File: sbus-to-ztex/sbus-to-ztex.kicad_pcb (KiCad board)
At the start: 4 copper layers, 99.7 x 83.8 mm, 37 parts, among them J1 Conn_01x06_Male, J2 47219-2001, J3 Conn_02x07_Odd_Even, J4 USB_B_Micro, J5 Conn_02x06_Odd_Even, U1 SN74CB3T16211DGGR, U2 SN74CB3T16211DGGR, U3 SN74CB3T16211DGGR, U4 SN74CB3T3125PW, U5 SN65220, U7 TPS2065

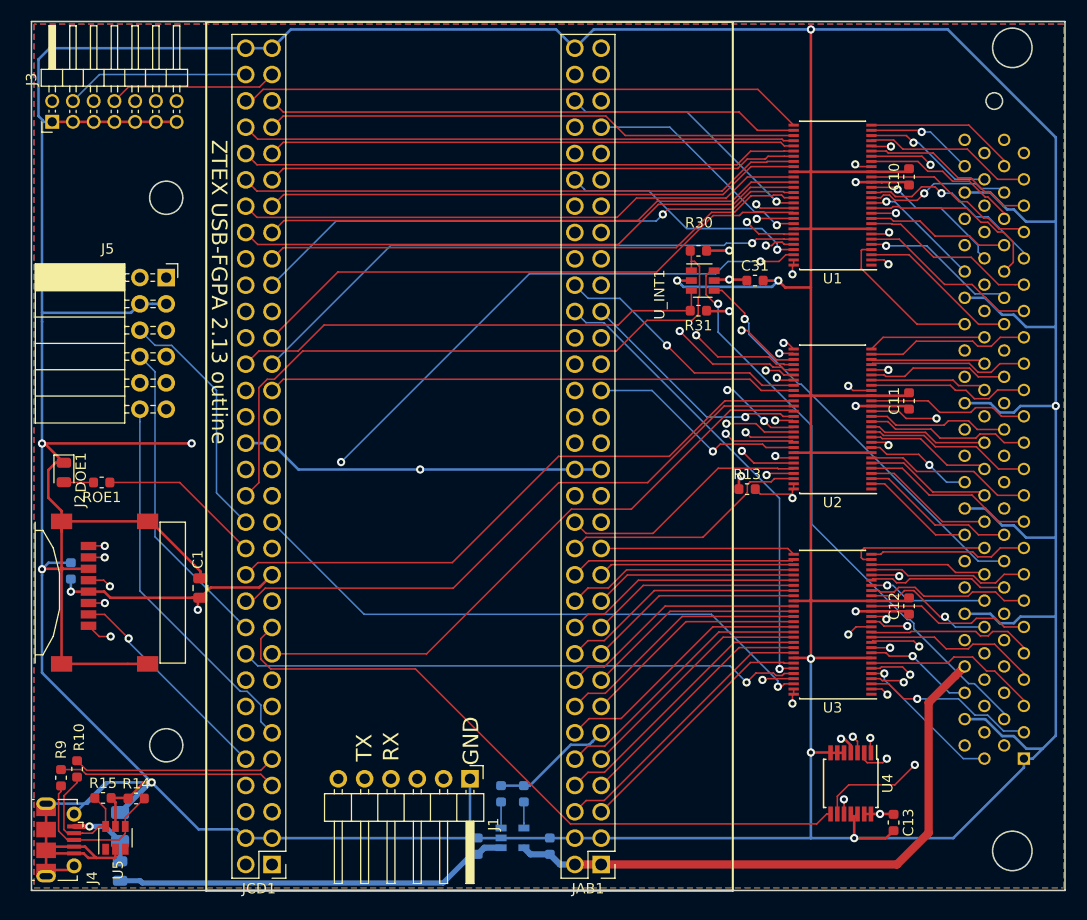
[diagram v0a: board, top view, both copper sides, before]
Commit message: fix footprints for SeeedStudio DRC results
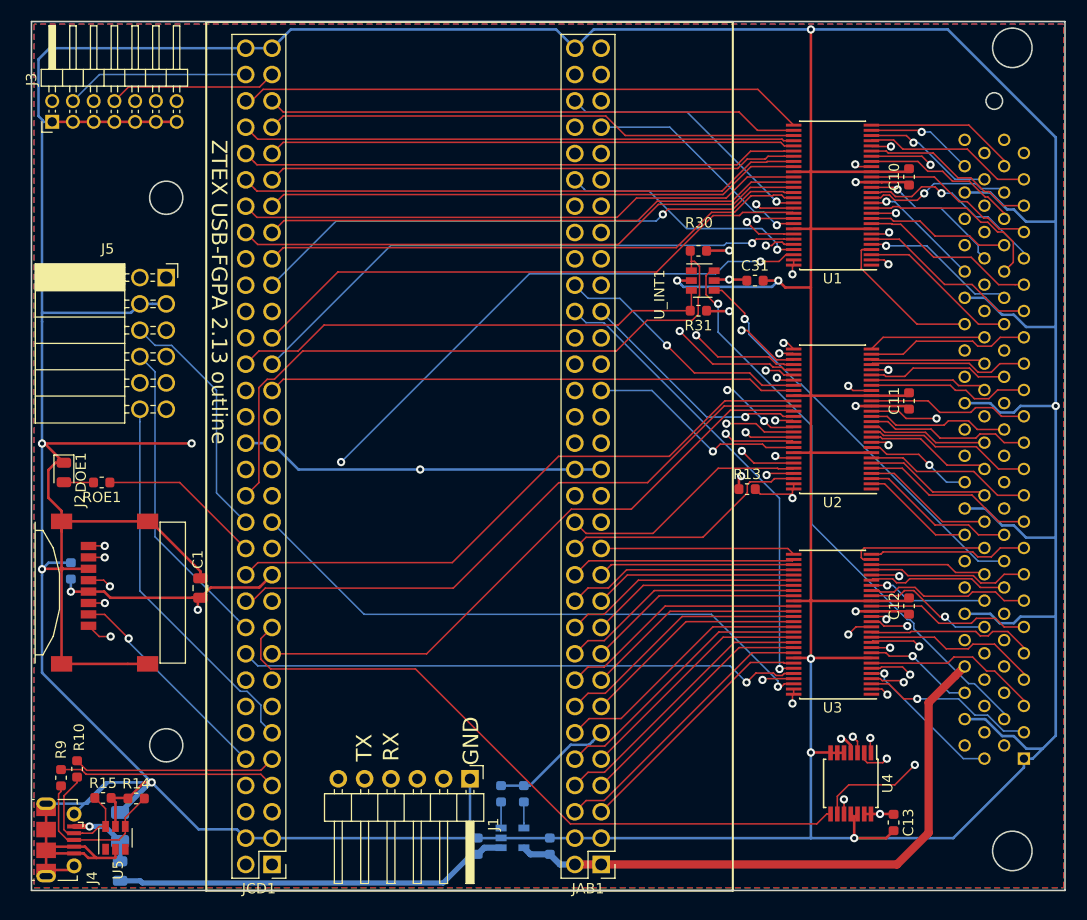
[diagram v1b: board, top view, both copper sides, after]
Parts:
- J3: footprint Connector_PinHeader_2.00mm:PinHeader_2x07_P2.00mm_Horizontal -> For_SeeedStudio:PinHeader_2x07_P2.00mm_Horizontal_For_SeeedStudio
- J5: footprint Connector_PinSocket_2.54mm:PinSocket_2x06_P2.54mm_Horizontal -> For_SeeedStudio:PinSocket_2x06_P2.54mm_Horizontal_For_SeeedStudio
- JAB1, JCD1: footprint Connector_PinHeader_2.54mm:PinHeader_2x32_P2.54mm_Vertical -> For_SeeedStudio:PinHeader_2x32_P2.54mm_Vertical_For_SeeedStudio
- U1, U2, U3: footprint Package_SO:TSSOP-56_6.1x14mm_P0.5mm -> For_SeeedStudio:TSSOP-56_6.1x14mm_P0.5mm_For_SeeedStudio

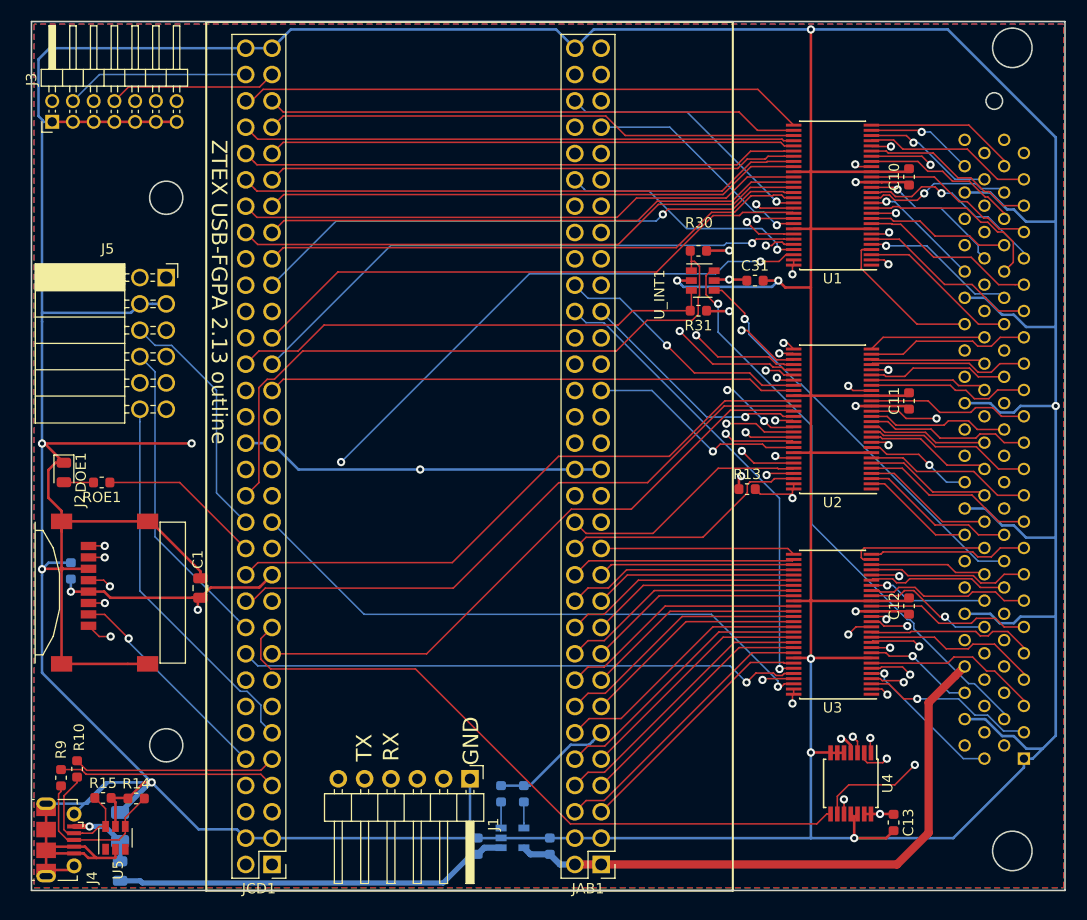
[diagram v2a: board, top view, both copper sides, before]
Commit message: update some MPN w/ SeeedStudio replacement
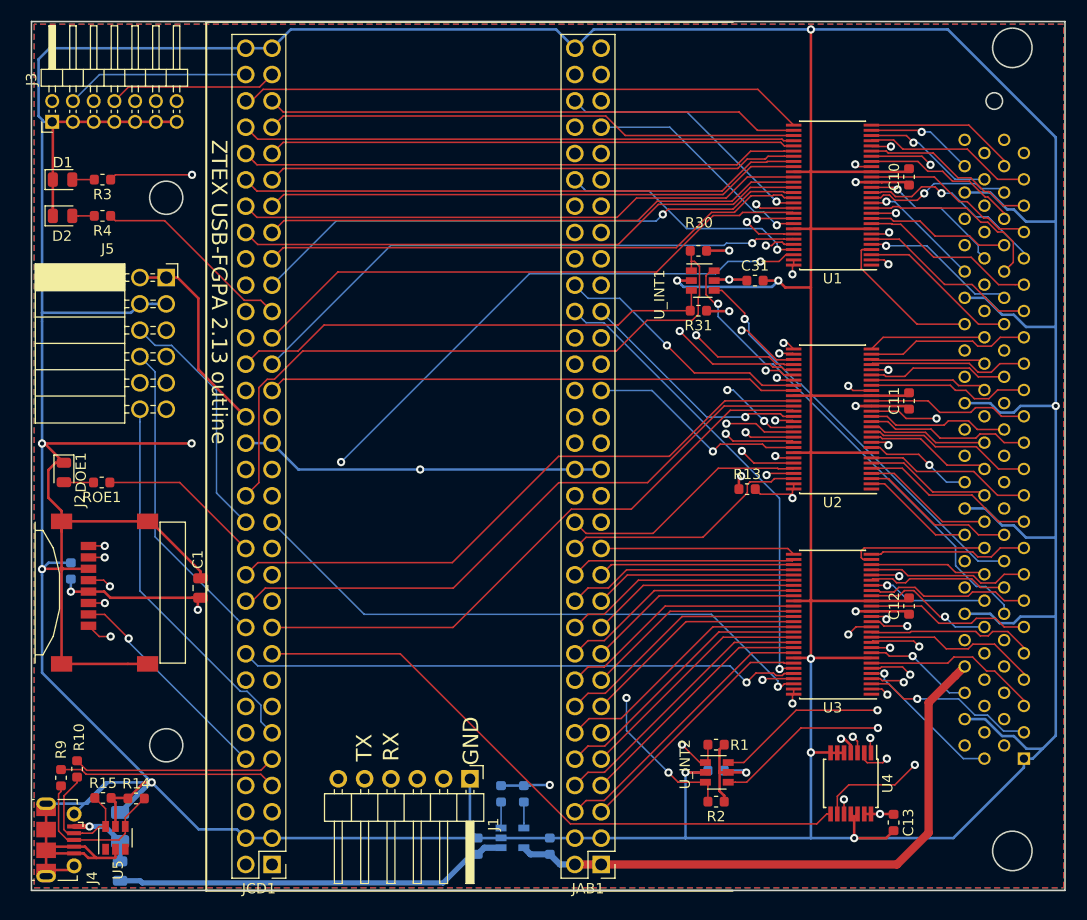
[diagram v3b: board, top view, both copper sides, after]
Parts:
- added C4: 100nF, Capacitor_SMD:C_0603_1608Metric, B.Cu at (163.0, 122.3)
- added D1: RED, LED_SMD:LED_0805_2012Metric, F.Cu at (100.0, 65.2)
- added D2: RED, LED_SMD:LED_0805_2012Metric, F.Cu at (100.0, 68.8)
- added R1: 10k, Resistor_SMD:R_0603_1608Metric, F.Cu at (163.0, 119.8)
- added R2: 10k, Resistor_SMD:R_0603_1608Metric, F.Cu at (163.0, 125.3)
- added R3: 549, Resistor_SMD:R_0603_1608Metric, F.Cu at (103.8, 65.2)
- added R4: 549, Resistor_SMD:R_0603_1608Metric, F.Cu at (103.8, 68.8)
- added U_INT2: 74LVC2G07, Package_TO_SOT_SMD:SOT-23-6, F.Cu at (163.1, 122.4)
- J1: footprint Connector_PinHeader_2.54mm:PinHeader_1x06_P2.54mm_Horizontal -> For_SeeedStudio:PinHeader_1x06_P2.54mm_Horizontal_For_SeeedStudio
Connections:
- JAB1 pad 11: +3V3 -> SBUS_3V3_INT[2]*
- JAB1 pad 49: +3V3 -> LED0
- JCD1 pad 17: SBUS_3V3_SIZ[0] -> SBUS_3V3_BG*
- JCD1 pad 19: SBUS_3V3_BG* -> SBUS_3V3_SIZ[0]
- JCD1 pad 23: +3V3 -> SBUS_3V3_INT[1]*
- JCD1 pad 30: SBUS_3V3_INT[1]* -> SBUS_3V3_INT[3]*
- JCD1 pad 43: +3V3 -> LED1
- R30 pad 2: SBUS_3V3_INT[1]* -> SBUS_3V3_INT[3]*
- U_INT1 pad 1: SBUS_3V3_INT[1]* -> SBUS_3V3_INT[3]*
- U_INT1 pad 6: SBUS_5V_INT[1]* -> SBUS_5V_INT[3]*
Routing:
- net SBUS_3V3_INT[3]*: track 0.00 -> 63.9 mm
- net LED0: track 0.00 -> 49.8 mm, vias 0 -> 1
- net SBUS_5V_INT[3]*: track 0.00 -> 46.6 mm, vias 0 -> 1
- net SBUS_5V_INT[2]*: track 0.00 -> 34.2 mm, vias 0 -> 1
- net SBUS_5V_INT[1]*: track 56.3 -> 29.1 mm
- net GND: track 743.0 -> 762.6 mm, vias 12 -> 13
- net LED1: track 0.00 -> 19.4 mm
- net SBUS_3V3_INT[2]*: track 0.00 -> 13.2 mm, vias 0 -> 1
- net SBUS_3V3_INT[1]*: track 63.9 -> 53.9 mm, vias 0 -> 2
- net +3V3: track 301.1 -> 294.8 mm, vias 11 -> 13
- net SBUS_3V3_BG*: track 65.4 -> 61.1 mm
- net Net-(D2-Pad2): track 0.00 -> 2.12 mm
- net Net-(D1-Pad2): track 0.00 -> 2.12 mm
- net SBUS_3V3_SIZ[0]: track 60.1 -> 59.0 mm
